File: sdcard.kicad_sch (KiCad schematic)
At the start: 2 parts, among them U3 sdcard

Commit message: friday changes
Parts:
- C4: DigiKey (none) -> 490-14466-2-ND; MPN (none) -> GRM21BR71C475KE51L; Manufacturer (none) -> Murata Electronics
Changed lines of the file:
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@@
+			)
+		)
+		(property "Manufacturer" "Murata Electronics"
+			(at 0 0 0)
+			(effects
+				(font
+					(size 1.27 1.27)
+				)
+				(hide yes)
+			)
+		)
+		(property "MPN" "GRM21BR71C475KE51L"
+			(at 0 0 0)
+			(effects
+				(font
+					(size 1.27 1.27)
+				)
+				(hide yes)
+			)
+		)
+		(property "DigiKey" "490-14466-2-ND"
+			(at 0 0 0)
+			(effects
+				(font
+					(size 1.27 1.27)
+				)
+				(hide yes)
 			)
 		)

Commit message: schematic updated
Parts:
- renumbered C4 to C41, U3 to U10
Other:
- moved on the sheet: C41, U10

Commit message: prettier schematic
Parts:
- U10: DigiKey (none) -> HR1964CT-ND; MPN (none) -> DM3AT-SF-PEJM5; Manufacturer (none) -> Hirose Electric Co Ltd
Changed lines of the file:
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@@
 			)
 		)
-		(property "Description" ""
+		(property "Description" "Socket microSD push-push R/A SMD"
 			(at 134.62 95.25 0)
 			(effects
@@
 			)
 		)
+		(property "DigiKey" "HR1964CT-ND"
+			(at 0 0 0)
+			(effects
+				(font
+					(size 1.27 1.27)
+				)
+				(hide yes)
+			)
+		)
+		(property "Manufacturer" "Hirose Electric Co Ltd"
+			(at 0 0 0)
+			(effects
+				(font
+					(size 1.27 1.27)
+				)
+				(hide yes)
+			)
+		)
+		(property "MPN" "DM3AT-SF-PEJM5"
+			(at 0 0 0)
+			(effects
+				(font
+					(size 1.27 1.27)
+				)
+				(hide yes)
+			)
+		)

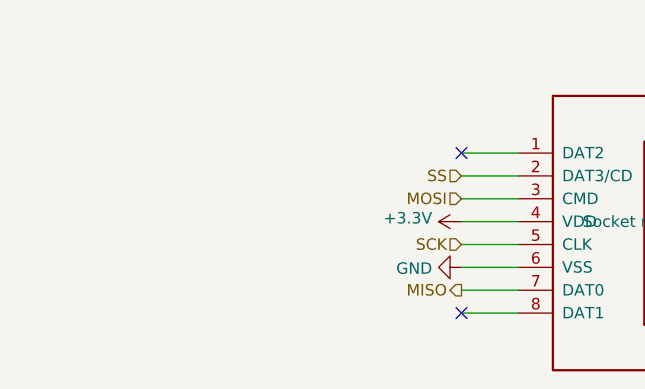
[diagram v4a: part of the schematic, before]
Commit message: 2 power source
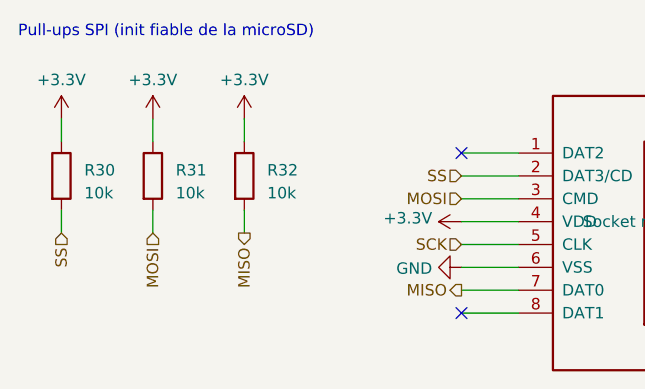
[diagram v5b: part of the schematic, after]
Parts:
- added R30, R31, R32: 10k, Resistor_SMD:R_0402_1005Metric, symbol Device:R
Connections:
- net +3.3V: now also R30.1, R31.1, R32.1
- net MISO: now also R32.2
- net MOSI: now also R31.2
- net SS: now also R30.2
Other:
- note added: "Pull-ups SPI (init fiable de la microSD)"

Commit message: last changes in work
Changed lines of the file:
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@@
 					(size 1.27 1.27)
 				)
+				(hide yes)
 			)
 		)
